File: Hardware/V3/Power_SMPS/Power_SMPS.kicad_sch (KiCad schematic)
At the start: 7 parts, among them J101 DIN41612_02x32_AC, J102 Conn_01x02, K101 ADW11, Q101 BSS138

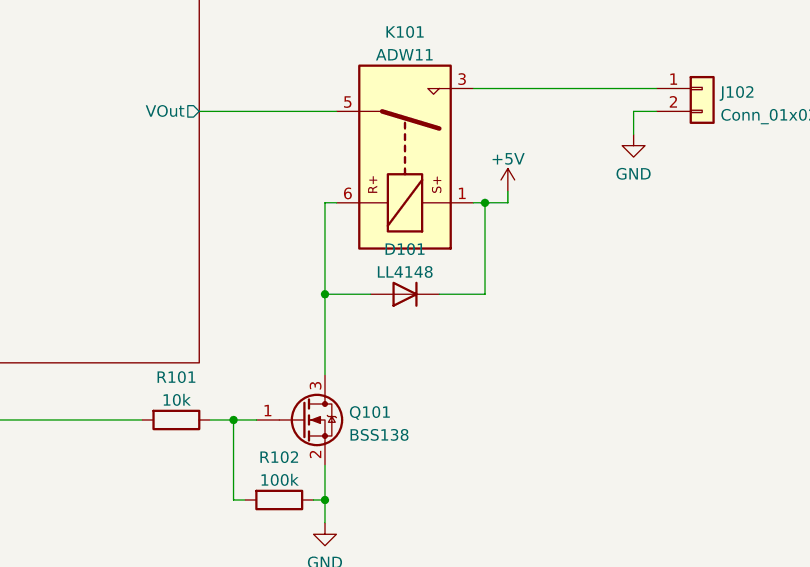
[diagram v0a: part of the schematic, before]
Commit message: SMPS Schematic and PCB Bugfix
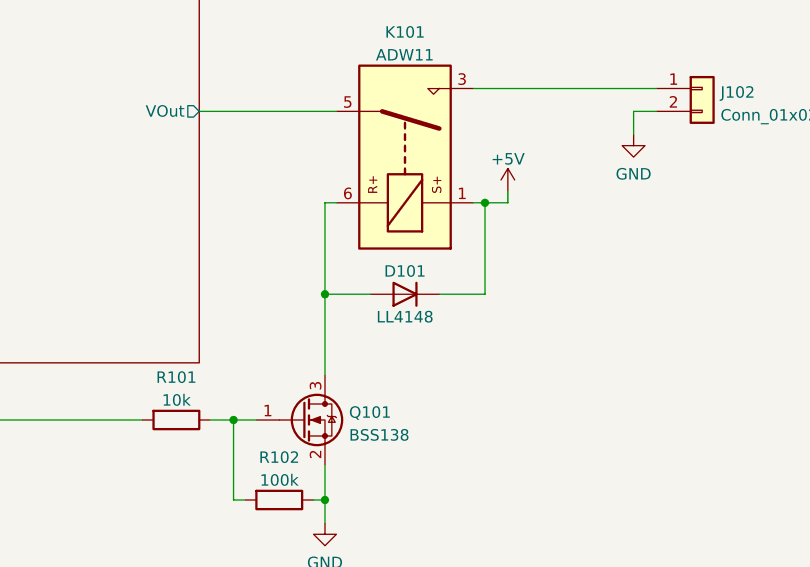
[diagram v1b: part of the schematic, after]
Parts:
- K101: footprint Relay_THT:Relay_1P1T_NO_10x24x18.8mm_Panasonic_ADW11xxxxW_THT -> eigene:JS 05 MN KT
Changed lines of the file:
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@@
     (property "Reference" "K101" (id 0) (at 347.98 120.7602 90))
     (property "Value" "ADW11" (id 1) (at 347.98 123.2971 90))
-    (property "Footprint" "Relay_THT:Relay_1P1T_NO_10x24x18.8mm_Panasonic_ADW11xxxxW_THT" (id 2) (at 346.71 100.965 0)
+    (property "Footprint" "eigene:JS 05 MN KT" (id 2) (at 346.71 100.965 0)
       (effects (font (size 1.27 1.27)) hide)
     )
@@
   )
   (symbol (lib_id "Diode:LL4148") (at 347.98 149.86 180) (unit 1)
-    (in_bom yes) (on_board yes) (fields_autoplaced)
-    (property "Reference" "D101" (id 0) (at 347.98 144.8902 0))
-    (property "Value" "LL4148" (id 1) (at 347.98 147.4271 0))
+    (in_bom yes) (on_board yes)
+    (property "Reference" "D101" (id 0) (at 347.98 147.32 0))
+    (property "Value" "LL4148" (id 1) (at 347.98 152.4 0))
     (property "Footprint" "Diode_SMD:D_MiniMELF" (id 2) (at 347.98 145.415 0)
       (effects (font (size 1.27 1.27)) hide)
@@
     )
     (path "/2b7fbaa7-69eb-431d-9dd7-d955aa1e6dc7"
-      (reference "K101") (unit 1) (value "ADW11") (footprint "Relay_THT:Relay_1P1T_NO_10x24x18.8mm_Panasonic_ADW11xxxxW_THT")
+      (reference "K101") (unit 1) (value "ADW11") (footprint "eigene:JS 05 MN KT")
     )
     (path "/80ecc604-5698-4185-9b84-236647b00752/b7c5248a-3f39-417b-84a0-bcbbfeefd2cf"
